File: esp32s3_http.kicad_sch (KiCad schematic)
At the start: 26 parts, among them J1 USB_B, J2 Jack-DC, SW1 SW_Push, SW2 SW_Push, U1 ESP32-S3-WROOM-1, U2 LF33_TO220, U3 LF50_TO220, Y1 32.768KHz

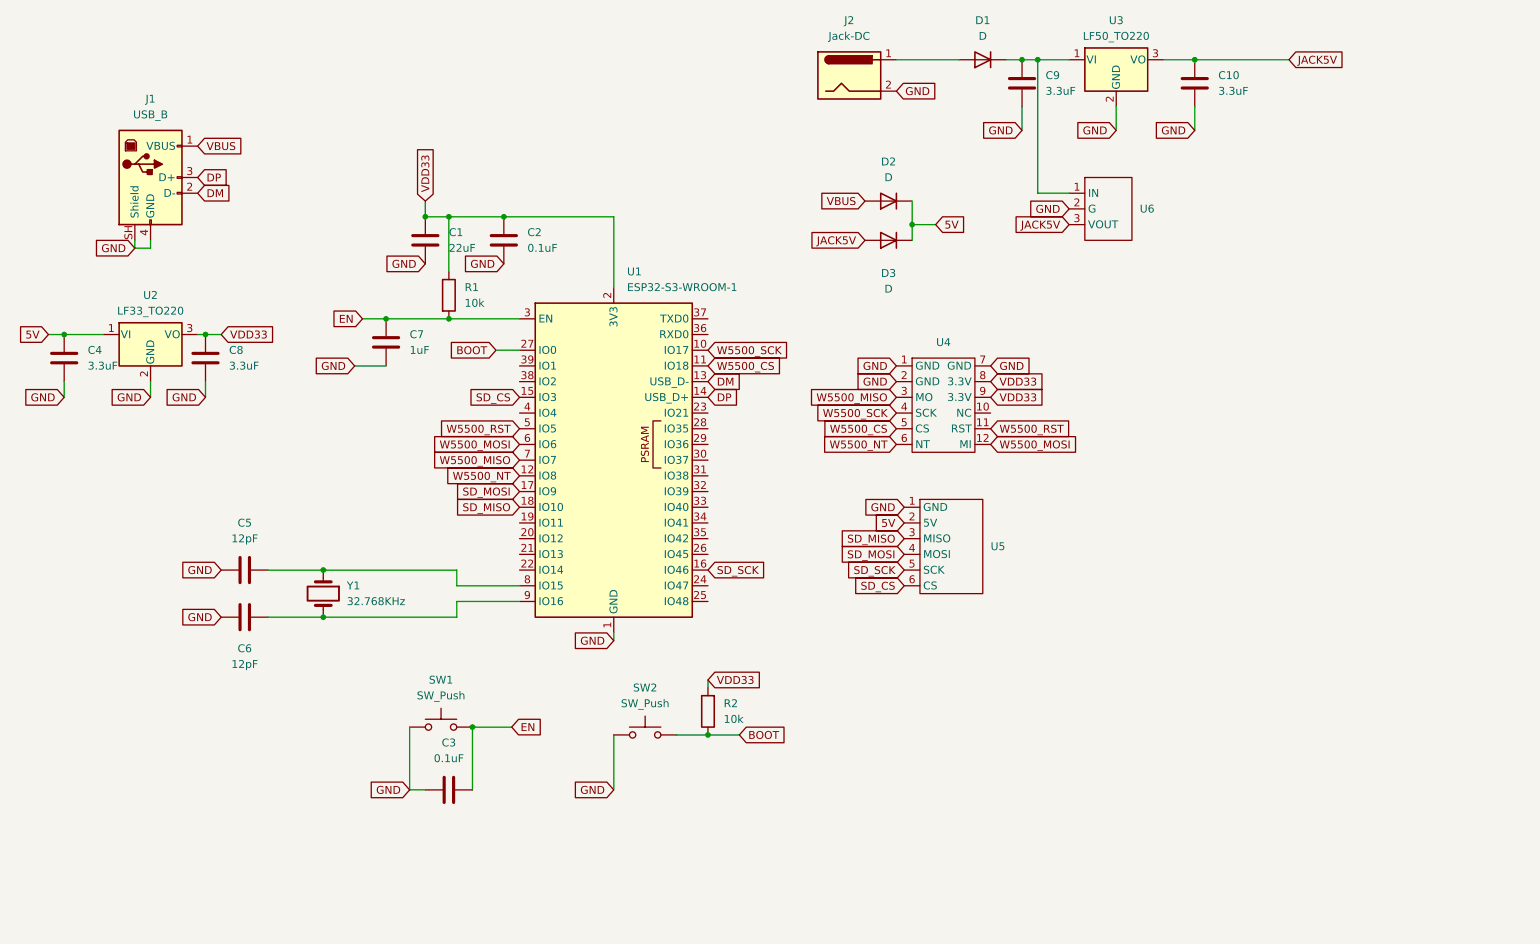
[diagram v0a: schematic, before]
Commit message: 回路図: 電源部品の見直し、SDピン移動、UARTヘッダ追加、ERCエラー解消
- D1-D3: 1N5819 (THT ショットキー, DO-41)
- U2: LM2940T-3.3, U3: NJM7805FA (TO-220F)
- C8: 47uF タンタル (LM2940 の出力 ESR 0.1-1Ω 要件)
- C1: 22uF/10V, 0805
- SD: IO3/IO46/IO9/IO10 -> IO9/IO10/IO11/IO12 (ストラッピングピン回避, 並び順は維持)
- J3: UART0 デバッグヘッダ (TX/RX/GND)
- 未使用ピンに未接続フラグ, PWR_FLAG 追加, U6 シンボルをライブラリと同期

Co-Authored-By: Claude Opus 5.5 <noreply@anthropic.com>
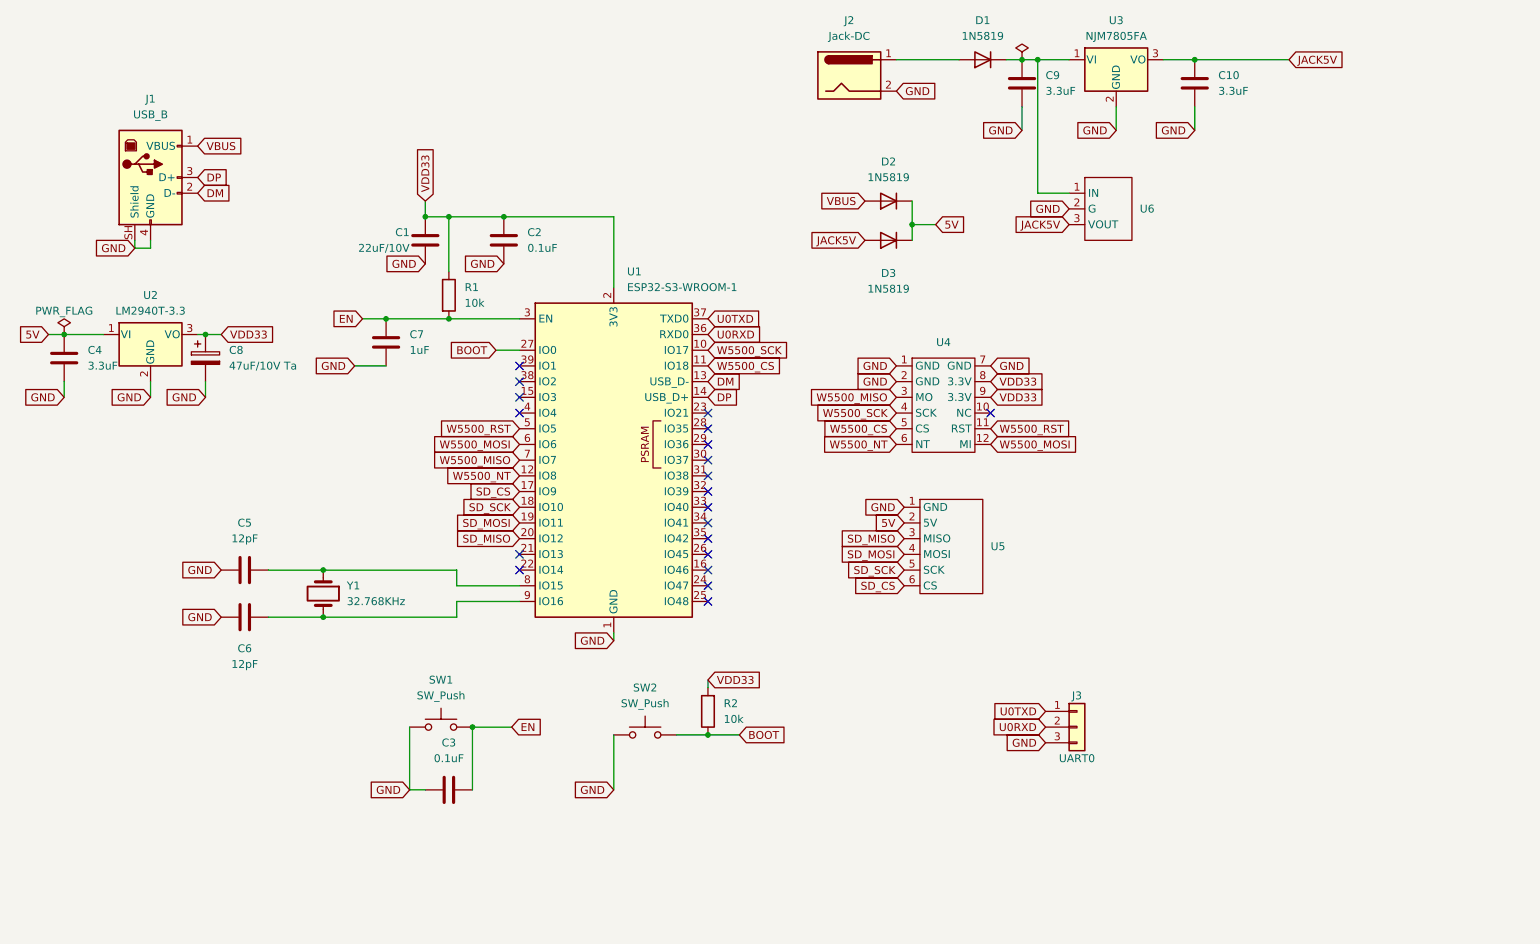
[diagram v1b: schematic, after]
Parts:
- added J3: UART0, Connector_PinHeader_2.54mm:PinHeader_1x03_P2.54mm_Vertical, symbol Connector_Generic:Conn_01x03
- C1: value 22uF -> 22uF/10V; footprint Capacitor_SMD:C_0603_1608Metric_Pad1.08x0.95mm_HandSolder -> Capacitor_SMD:C_0805_2012Metric_Pad1.18x1.45mm_HandSolder
- C8: value 3.3uF -> 47uF/10V Ta; footprint Capacitor_SMD:C_0603_1608Metric_Pad1.08x0.95mm_HandSolder -> Capacitor_Tantalum_SMD:CP_EIA-3528-21_Kemet-B_HandSolder; symbol Device:C -> Device:C_Polarized
- D1, D2, D3: value D -> 1N5819; footprint Diode_SMD:D_0603_1608Metric_Pad1.05x0.95mm_HandSolder -> Diode_THT:D_DO-41_SOD81_P7.62mm_Horizontal
- U2: value LF33_TO220 -> LM2940T-3.3
- U3: value LF50_TO220 -> NJM7805FA; footprint Package_TO_SOT_THT:TO-220-3_Vertical -> Package_TO_SOT_THT:TO-220F-3_Vertical
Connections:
- net GND: now also C8.2, J3.3 (Pin_3); no longer C8.1
- net SD_CS: now also U1.17 (IO9); no longer U1.15 (IO3)
- net SD_MISO: now also U1.20 (IO12); no longer U1.18 (IO10)
- net SD_MOSI: now also U1.19 (IO11); no longer U1.17 (IO9)
- net SD_SCK: now also U1.18 (IO10); no longer U1.16 (IO46)
- net VDD33: now also C8.1; no longer C8.2
- net U0RXD: now reaches U1.36 (RXD0)
- net U0RXD: now also J3.2 (Pin_2)
- net U0TXD: now reaches U1.37 (TXD0)
- net U0TXD: now also J3.1 (Pin_1)
- no-connect marks 0 -> 20

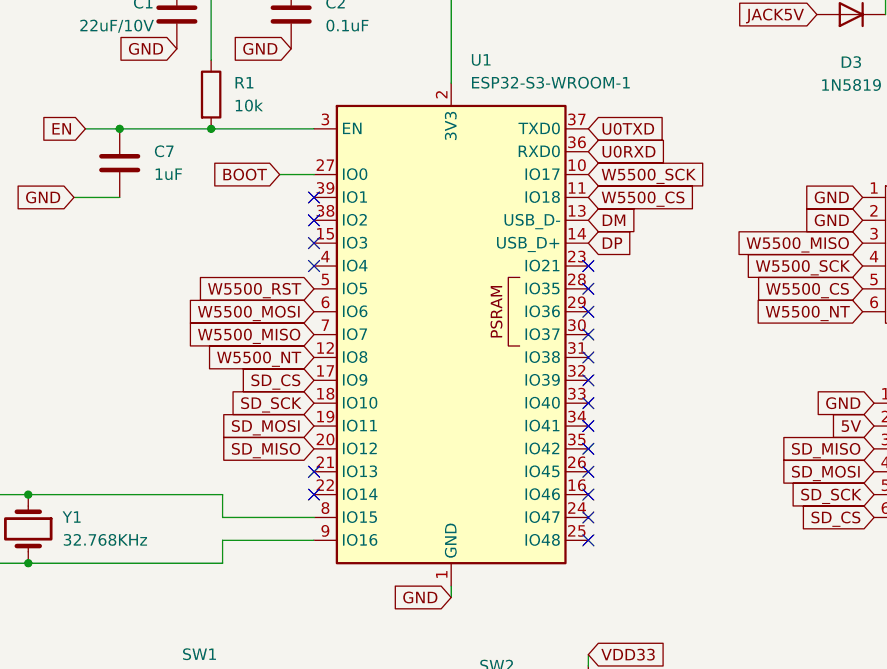
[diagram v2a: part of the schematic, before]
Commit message: PCB: W5500/SD のピン割当を配線向きに変更、EN/デカップリング集約、GND ステッチング
- W5500: IO9-IO14 (U1 左辺), SD: IO38-IO41 (U1 下辺, U5 直上)
- C2 を U1 pin1/2 直上に、EN 回路を pin3 直上に集約
- U1 EPAD サーマルビア 0.2 -> 0.3mm
- Power/GND ネットクラス (0.6mm) 追加

Co-Authored-By: Claude Opus 5.5 <noreply@anthropic.com>
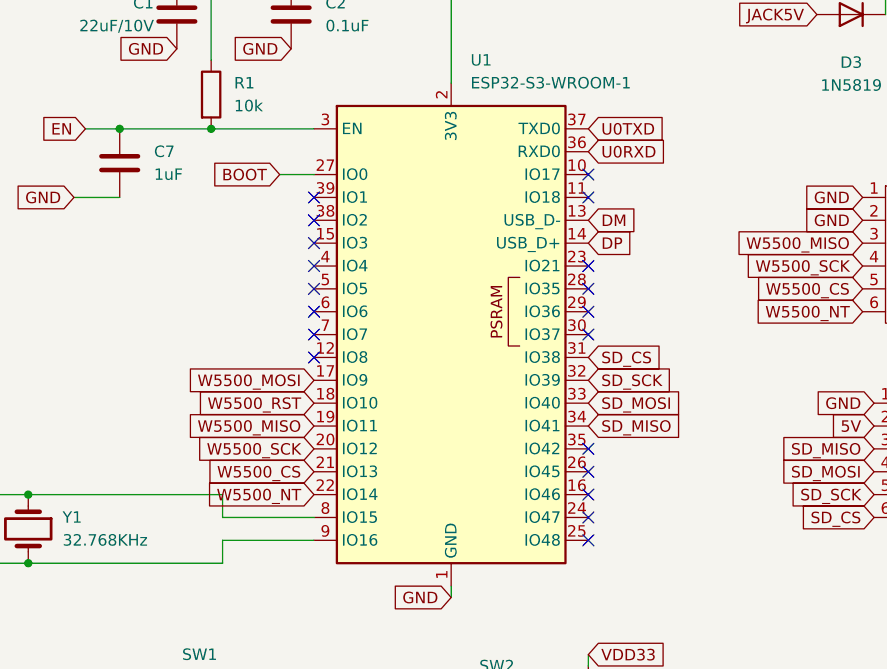
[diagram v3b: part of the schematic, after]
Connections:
- net SD_CS: now also U1.31 (IO38); no longer U1.17 (IO9)
- net SD_MISO: now also U1.34 (IO41); no longer U1.20 (IO12)
- net SD_MOSI: now also U1.33 (IO40); no longer U1.19 (IO11)
- net SD_SCK: now also U1.32 (IO39); no longer U1.18 (IO10)
- net W5500_CS: now also U1.21 (IO13); no longer U1.11 (IO18)
- net W5500_MISO: now also U1.19 (IO11); no longer U1.7 (IO7)
- net W5500_MOSI: now also U1.17 (IO9); no longer U1.6 (IO6)
- net W5500_NT: now also U1.22 (IO14); no longer U1.12 (IO8)
- net W5500_RST: now also U1.18 (IO10); no longer U1.5 (IO5)
- net W5500_SCK: now also U1.20 (IO12); no longer U1.10 (IO17)

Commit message: 回路図: OS-CON 1000uF (6SEPC1000MD) を W5500 と ESP32 の VDD33 に追加
Co-Authored-By: Claude Opus 5.5 <noreply@anthropic.com>
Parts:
- added C11, C12: 1000uF/6.3V OS-CON, Capacitor_THT:CP_Radial_D8.0mm_P3.50mm, symbol Device:C_Polarized
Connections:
- net GND: now also C11.2, C12.2
- net VDD33: now also C11.1, C12.1

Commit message: 回路図: 動作確認用 LED (PWR/3V3/STAT/LAN/SD) を追加
- D4 PWR(5V), D5 3V3, D6 STAT(IO21), D7 LAN(W5500_CS アクティブ), D8 SD(SD_CS アクティブ)
- LED は 3mm THT、抵抗は 0603

Co-Authored-By: Claude Opus 5.5 <noreply@anthropic.com>
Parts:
- added D4: Red, LED_THT:LED_D3.0mm, symbol Device:LED
- added D5: Green, LED_THT:LED_D3.0mm, symbol Device:LED
- added D6: Yellow, LED_THT:LED_D3.0mm, symbol Device:LED
- added D7, D8: Orange, LED_THT:LED_D3.0mm, symbol Device:LED
- added R4: 2.2k, Resistor_SMD:R_0603_1608Metric_Pad0.98x0.95mm_HandSolder, symbol Device:R
- added R5, R6, R7, R8: 1k, Resistor_SMD:R_0603_1608Metric_Pad0.98x0.95mm_HandSolder, symbol Device:R
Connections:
- net 5V: now also R4.1
- net GND: now also D4.1 (K), D5.1 (K), D6.1 (K)
- net SD_CS: now also D8.1 (K)
- net VDD33: now also R5.1, R7.1, R8.1
- net W5500_CS: now also D7.1 (K)
- net LED_STAT: now reaches U1.23 (IO21)
- net LED_STAT: now also R6.1
- new net: D4.2 (A), R4.2
- new net: D5.2 (A), R5.2
- new net: D8.2 (A), R8.2
- new net: D7.2 (A), R7.2
- new net: D6.2 (A), R6.2
- no-connect marks 20 -> 19

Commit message: PCB: 動作確認用 LED を追加
- PWR/3V3/STAT を左端パネルに、LAN は W5500 バス下、SD は U5 横に配置
- LAN/SD は VDD33→LED→R→CS 構成 (アノードを近傍の VDD33 に直結)

Co-Authored-By: Claude Opus 5.5 <noreply@anthropic.com>
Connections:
- net SD_CS: now also R8.2; no longer D8.1 (K)
- net VDD33: now also D7.2 (A), D8.2 (A); no longer R7.1, R8.1
- net W5500_CS: now also R7.2; no longer D7.1 (K)
- new net: D8.1 (K), R8.1
- new net: D7.1 (K), R7.1
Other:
- moved on the sheet: D7, D8, R7, R8
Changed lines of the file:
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@@
 	(symbol
 		(lib_id "Device:R")
-		(at 238.76 130.81 0)
+		(at 238.76 138.43 0)
 		(unit 1)
 		(body_style 1)
@@
 		(dnp no)
 		(property "Reference" "R7"
-			(at 242.57 129.54 0)
+			(at 242.57 137.16 0)
 			(show_name no)
 			(do_not_autoplace no)
@@
 		)
 		(property "Value" "1k"
-			(at 242.57 132.08 0)
+			(at 242.57 139.70 0)
 			(show_name no)
 			(do_not_autoplace no)
@@
 		)
 		(property "Footprint" "Resistor_SMD:R_0603_1608Metric_Pad0.98x0.95mm_HandSolder"
-			(at 238.76 130.81 0)
+			(at 238.76 138.43 0)
 			(hide yes)
 			(show_name no)
@@
 		)
 		(property "Datasheet" ""
-			(at 238.76 130.81 0)
+			(at 238.76 138.43 0)
 			(hide yes)
 			(show_name no)
@@
 		)
 		(property "Description" "Resistor"
-			(at 238.76 130.81 0)
+			(at 238.76 138.43 0)
 			(hide yes)
 			(show_name no)
@@
 	(symbol
 		(lib_id "Device:LED")
-		(at 238.76 138.43 90)
+		(at 238.76 130.81 90)
 		(unit 1)
 		(body_style 1)
@@
 		(dnp no)
 		(property "Reference" "D7"
-			(at 242.57 137.16 90)
+			(at 242.57 129.54 90)
 			(show_name no)
 			(do_not_autoplace no)
@@
 		)
 		(property "Value" "Orange"
-			(at 242.57 139.7 90)
+			(at 242.57 132.08 90)
 			(show_name no)
 			(do_not_autoplace no)
@@
 		)
 		(property "Footprint" "LED_THT:LED_D3.0mm"
-			(at 238.76 138.43 0)
+			(at 238.76 130.81 0)
 			(hide yes)
 			(show_name no)
@@
 		)
 		(property "Datasheet" ""
-			(at 238.76 138.43 0)
+			(at 238.76 130.81 0)
 			(hide yes)
 			(show_name no)
@@
 		)
 		(property "Description" "3mm THT LED Orange, indicator: LAN"
-			(at 238.76 138.43 0)
+			(at 238.76 130.81 0)
 			(hide yes)
 			(show_name no)
@@
 	(symbol
 		(lib_id "Device:R")
-		(at 251.46 130.81 0)
+		(at 251.46 138.43 0)
 		(unit 1)
 		(body_style 1)
@@
 		(dnp no)
 		(property "Reference" "R8"
-			(at 255.27 129.54 0)
+			(at 255.27 137.16 0)
 			(show_name no)
 			(do_not_autoplace no)
@@
 		)
 		(property "Value" "1k"
-			(at 255.27 132.08 0)
+			(at 255.27 139.70 0)
 			(show_name no)
 			(do_not_autoplace no)
@@
 		)
 		(property "Footprint" "Resistor_SMD:R_0603_1608Metric_Pad0.98x0.95mm_HandSolder"
-			(at 251.46 130.81 0)
+			(at 251.46 138.43 0)
 			(hide yes)
 			(show_name no)
@@
 		)
 		(property "Datasheet" ""
-			(at 251.46 130.81 0)
+			(at 251.46 138.43 0)
 			(hide yes)
 			(show_name no)
@@
 		)
 		(property "Description" "Resistor"
-			(at 251.46 130.81 0)
+			(at 251.46 138.43 0)
 			(hide yes)
 			(show_name no)
@@
 	(symbol
 		(lib_id "Device:LED")
-		(at 251.46 138.43 90)
+		(at 251.46 130.81 90)
 		(unit 1)
 		(body_style 1)
@@
 		(dnp no)
 		(property "Reference" "D8"
-			(at 255.27 137.16 90)
+			(at 255.27 129.54 90)
 			(show_name no)
 			(do_not_autoplace no)
@@
 		)
 		(property "Value" "Orange"
-			(at 255.27 139.7 90)
+			(at 255.27 132.08 90)
 			(show_name no)
 			(do_not_autoplace no)
@@
 		)
 		(property "Footprint" "LED_THT:LED_D3.0mm"
-			(at 251.46 138.43 0)
+			(at 251.46 130.81 0)
 			(hide yes)
 			(show_name no)
@@
 		)
 		(property "Datasheet" ""
-			(at 251.46 138.43 0)
+			(at 251.46 130.81 0)
 			(hide yes)
 			(show_name no)
@@
 		)
 		(property "Description" "3mm THT LED Orange, indicator: SD"
-			(at 251.46 138.43 0)
-			(hide yes)
-			(show_name no)
+			(at 251.46 130.81 0)
+			(hide yes)
+			(show_name no)
